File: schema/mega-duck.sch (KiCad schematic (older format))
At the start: 12 parts, among them J1 USB_A, SW1 ON/OFF, U1 ATmega8A-AU, Y1 16Mhz

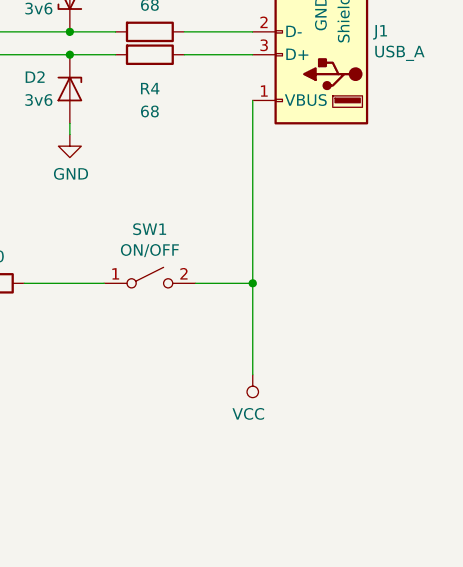
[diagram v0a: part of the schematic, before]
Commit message: Added capacitor to schema.
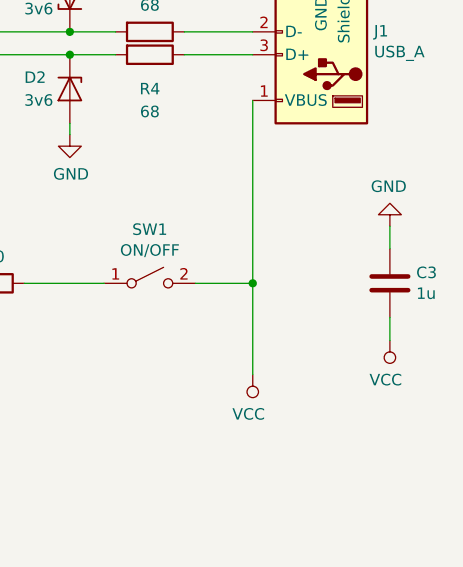
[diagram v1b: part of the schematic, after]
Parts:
- added C3: 1u, symbol Device:C
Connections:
- net GND: now also C3.1
- net VCC: now also C3.2
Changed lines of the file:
@@
 EESchema Schematic File Version 4
+LIBS:mega-duck-cache
 EELAYER 30 0
 EELAYER END
@@
 Text Label 6800 3100 0    50   ~ 0
 D+
+$Comp
+L power:GND #PWR010
+U 1 1 5DC9EFA0
+P 9900 3350
+F 0 "#PWR010" H 9900 3100 50  0001 C CNN
+F 1 "GND" H 9905 3177 50  0000 C CNN
+F 2 "" H 9900 3350 50  0001 C CNN
+F 3 "" H 9900 3350 50  0001 C CNN
+	1    9900 3350
+	-1   0    0    1
+$EndComp
+$Comp
+L power:VCC #PWR011
+U 1 1 5DC9F8CE
+P 9900 3850
+F 0 "#PWR011" H 9900 3700 50  0001 C CNN
+F 1 "VCC" H 9918 4023 50  0000 C CNN
+F 2 "" H 9900 3850 50  0001 C CNN
+F 3 "" H 9900 3850 50  0001 C CNN
+	1    9900 3850
+	-1   0    0    1
+$EndComp
+$Comp
+L Device:C C3
+U 1 1 5DC9FC9A
+P 9900 3600
+F 0 "C3" H 10015 3646 50  0000 L CNN
+F 1 "1u" H 10015 3555 50  0000 L CNN
+F 2 "" H 9938 3450 50  0001 C CNN
+F 3 "~" H 9900 3600 50  0001 C CNN
+	1    9900 3600
+	1    0    0    -1
+$EndComp
+Wire Wire Line
+	9900 3350 9900 3450
+Wire Wire Line
+	9900 3750 9900 3850
 $EndSCHEMATC
